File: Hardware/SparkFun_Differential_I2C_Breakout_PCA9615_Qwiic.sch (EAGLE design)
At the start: 40 parts, among them J3 RJ45, U1 PCA9615

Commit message: Pushing design before Redboard Review
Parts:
- removed LOGO2: SFE_LOGO_NAME.1_INCH, SparkFun-Aesthetics:SFE_LOGO_NAME.1_INCH
- removed R1A, R2A, R3A, R4A, R5A, R6A: DNP, SparkFun-Resistors:RESISTORAXIAL-0.3
- added J5: (no value), SparkFun-Connectors:CONN_01
- R1, R3, R4, R6: value 750 -> 390; device SparkFun-Resistors:750OHM-0603-1/10W-1% -> SparkFun-Resistors:390OHM-0603-1/10W-1%
- R2, R5: value 750 -> 100; device SparkFun-Resistors:750OHM-0603-1/10W-1% -> SparkFun-Resistors:100OHM-0603-1/10W-1%
- renumbered JP6 to J6
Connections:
- net DSCL+: no longer R1A.1, R2A.2
- net DSCL-: no longer R2A.1, R3A.2
- net DSDA+: no longer R4A.1, R5A.2
- net DSDA-: no longer R5A.1, R6A.2
- net EN: now also J5.1; no longer J4.1
- net GND: now also J4.1; no longer R3A.1, R6A.1
- net VDD_B: no longer R1A.2, R4A.2
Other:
- note removed: "These Resistor values are arbitrariy until testing can be performed on the protos."
- moved on the sheet: J4

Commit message: Adding PCA9615 to SFE Eagle Library
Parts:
- U1: device Openponics:PCA9615 -> SparkFun-IC-Comms:PCA9615
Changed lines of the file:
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@@
 <part name="J1" library="SparkFun-Connectors" deviceset="QWIIC_CONNECTOR" device="JS-1MM"/>
 <part name="GND1" library="SparkFun-PowerSymbols" deviceset="GND" device=""/>
-<part name="U1" library="Openponics" deviceset="PCA9615" device=""/>
+<part name="U1" library="SparkFun-IC-Comms" deviceset="PCA9615" device=""/>
 <part name="J2" library="SparkFun-Connectors" deviceset="QWIIC_CONNECTOR" device="JS-1MM"/>
 <part name="GND2" library="SparkFun-PowerSymbols" deviceset="GND" device=""/>

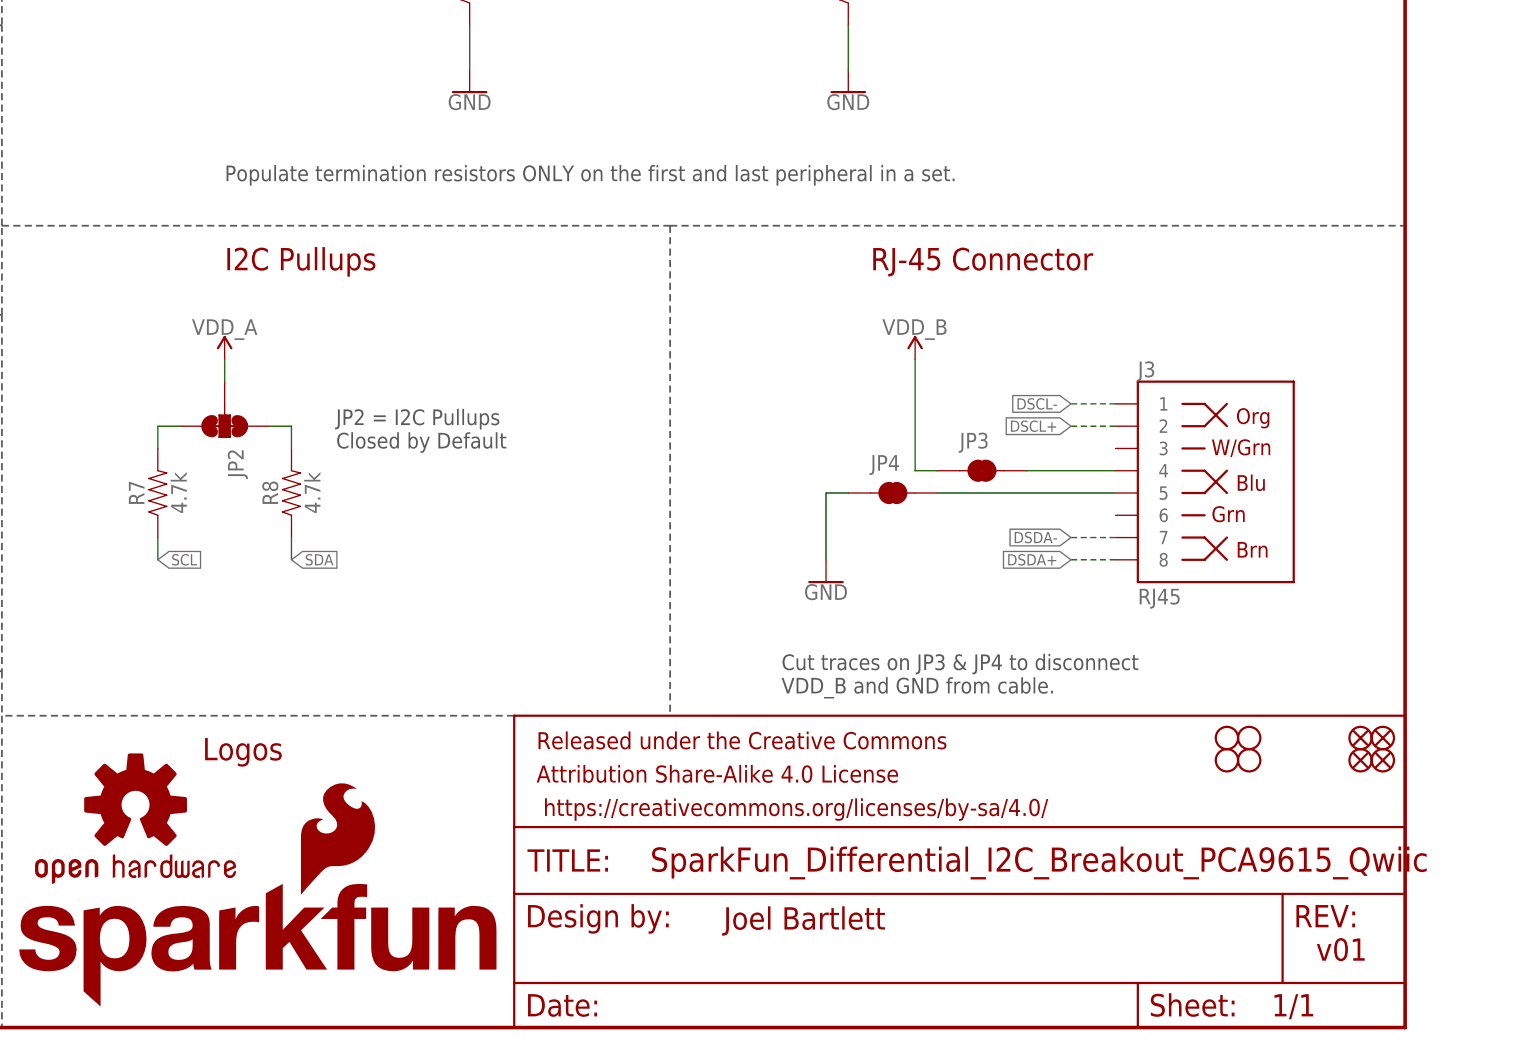
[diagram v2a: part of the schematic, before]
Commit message: ENG Design Checklist changes
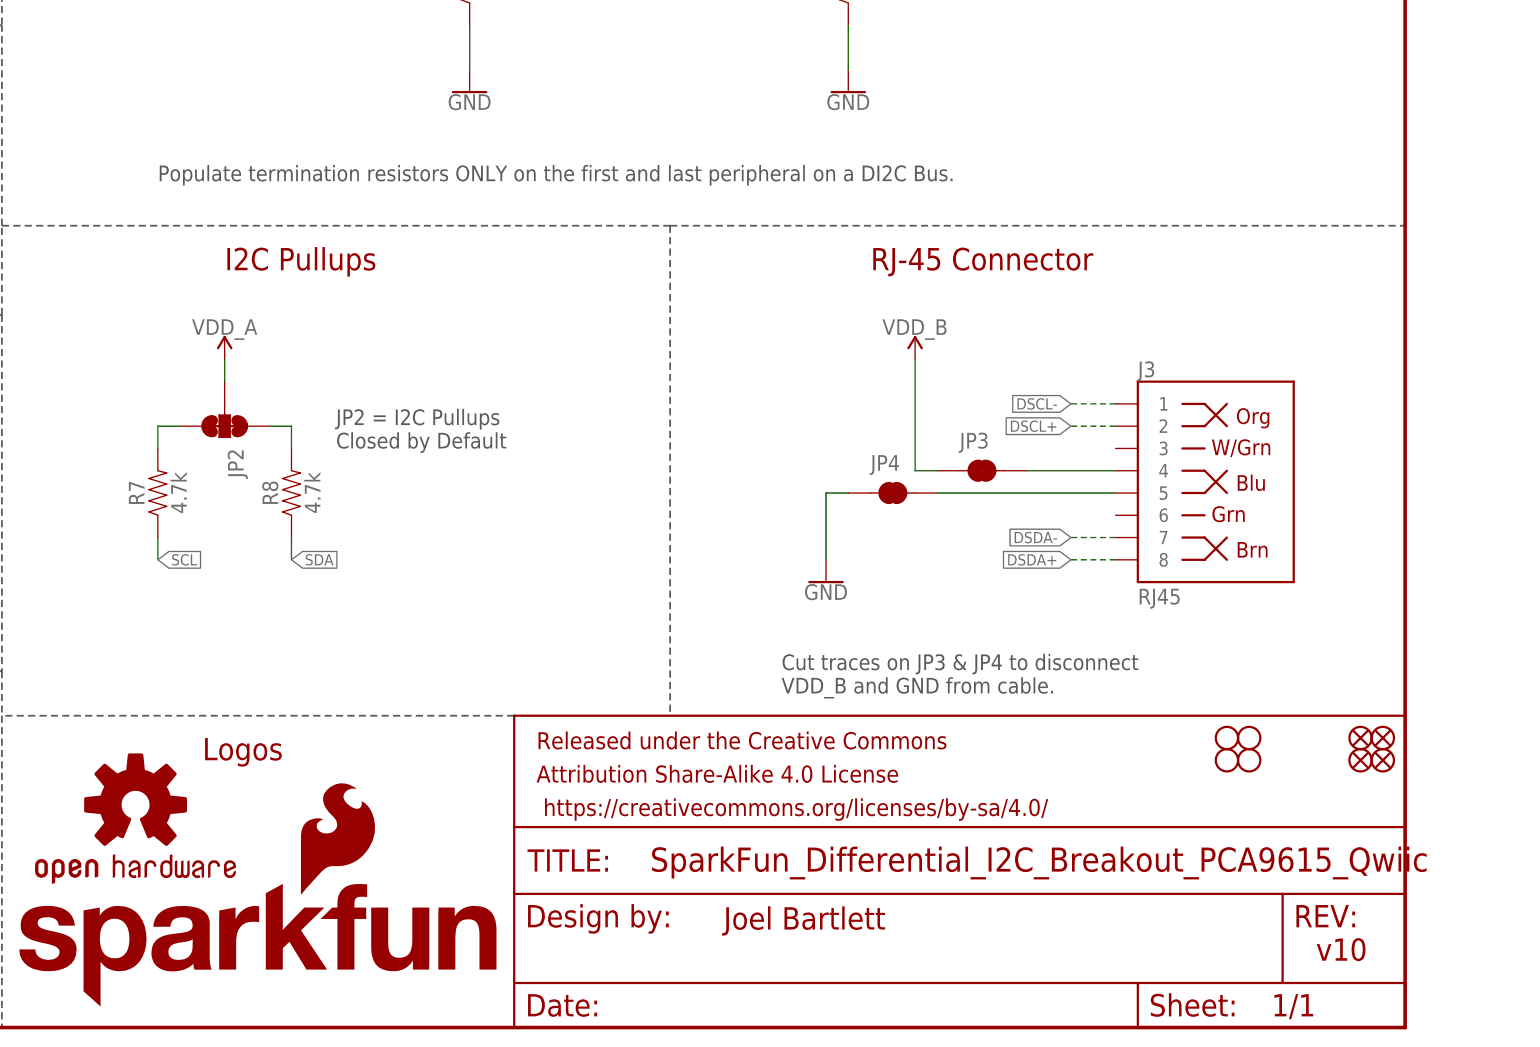
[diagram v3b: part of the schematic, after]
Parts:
- J4: device SparkFun-Connectors:CONN_02 -> SparkFun-Connectors:CONN_021X02_NO_SILK
- J5: device SparkFun-Connectors:CONN_01 -> SparkFun-Connectors:CONN_01PTH_NO_SILK_YES_STOP
- J6: device SparkX:I2C_STANDARDSILK -> SparkX:I2C_STANDARD_NO_SILK
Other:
- note added: "Populate termination resistors ONLY on the first and last peripheral on a DI2C Bus."
- note added: "v10"
- note removed: "Populate termination resistors ONLY on the first and last peripheral in a set."
- note removed: "v01"
